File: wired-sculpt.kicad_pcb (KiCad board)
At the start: 2 copper layers, 40 x 54 mm, 39 parts, among them J1 USB Micro, J2 FFC 30pin, J3 AVR-ISP-6 - NOT FITTED, Q1 P-MOSFET, Q2 N-MOSFET, SW1 Button, SW2 JST connector, U1 ESD Protection, U2 LM2776DBVT, U3 AT90USB1286-AU, Y1 Crystal 16MHz

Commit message: Copy MPN back to Value field
This is for compatbility with the JLCPCB plugin
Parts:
- C1: value 4.7uF -> CL21A475KOFNNNE
- C10, C11, C12: value 0.1uF -> CL10B104KB8NNNC
- C2: value 0.1uF -> CL21B104KACNNNC
- C3: value 10nF -> CL21B103KBANNNC
- C4, C5, C6, C9: value 1uF -> CL10A105KA8NNNC
- C7, C8: value 16pF -> CL10C160JB8NNNC
- D1: value green led -> 150080GS75000
- J1: value USB Micro -> 10103594-0001LF
- J2: value FFC 30pin -> FFC3B07-30-T
- Q1: value P-MOSFET -> BSS84AK,215
- Q2: value N-MOSFET -> 2N7002BK
- R1, R2, R7: value 22 -> ERJ-PA3F22R0V
- R10, R6, R9: value 330 -> ERJ-3GEYJ331V
- R11, R12: value 150 -> ERJ-PA3J151V
- R3, R8: value 4.7k -> ERJ-PA3J472V
- R4: value 887k -> ERJ-3EKF8873V
- R5: value 47k -> ERJ-PA3J473V
- SW1: value Button -> FSMSM
- SW2: value JST connector -> S2B-PH-K-S(LF)(SN)
- U1: value ESD Protection -> USBLC6-2SC6
- Y1: value Crystal 16MHz -> TSX-3225 16.0000MF18X-AC0

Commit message: Change microcontroller and one FET MPN
Fixes mismatch that PCBWay flagged
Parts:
- Q2: value 2N7002BK -> 2N7002BK,215
- U3: value AT90USB1286-AU -> AT90USB1286-AUR
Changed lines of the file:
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@@
     (descr "64-Lead Plastic Thin Quad Flatpack (PF) - 14x14x1 mm Body, 2.00 mm [TQFP] (see Microchip Packaging Specification 00000049BS.pdf)")
     (tags "QFP 0.8")
-    (property "MPN" "AT90USB1286-AU")
+    (property "MPN" "AT90USB1286-AUR")
     (property "Sheetfile" "wired-sculpt.kicad_sch")
     (property "Sheetname" "")
@@
       (effects (font (size 1 1) (thickness 0.15)))
     )
-    (fp_text value "AT90USB1286-AU" (at 0 9.45) (layer "F.Fab")
+    (fp_text value "AT90USB1286-AUR" (at 0 9.45) (layer "F.Fab")
       (effects (font (size 1 1) (thickness 0.15)))
     )
@@
     (descr "SOT-23, Standard")
     (tags "SOT-23")
-    (property "MPN" "2N7002BK")
+    (property "MPN" "2N7002BK,215")
     (property "Notes" "N-MOSFET")
     (property "Sheetfile" "wired-sculpt.kicad_sch")
@@
       (effects (font (size 1 1) (thickness 0.15)))
     )
-    (fp_text value "2N7002BK" (at 0 2.5) (layer "F.Fab")
-      (effects (font (size 1 1) (thickness 0.15)))
-    )
+    (fp_text value "2N7002BK,215" (at 0 2.5) (layer "F.Fab")
+      (effects (font (size 1 1) (thickness 0.15)))
+    )

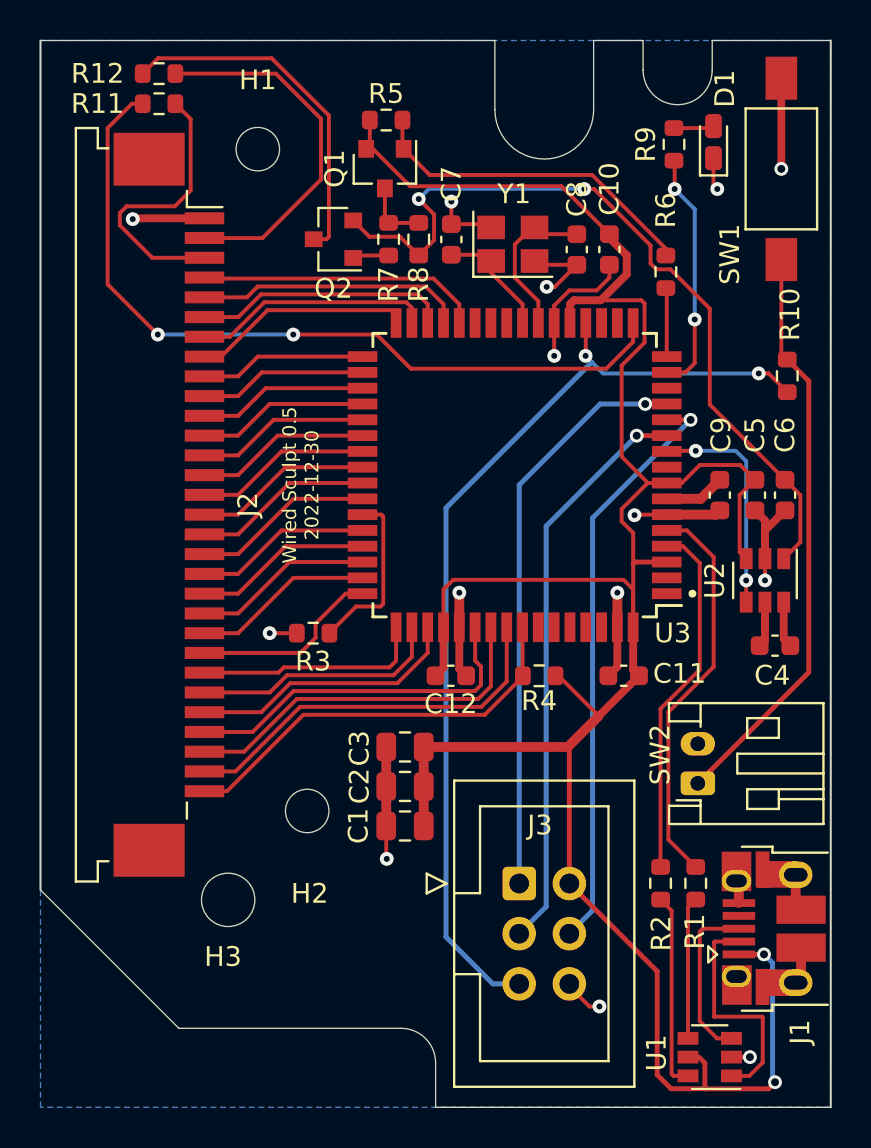
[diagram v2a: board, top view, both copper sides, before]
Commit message: Properly ground mounting pads for FFC
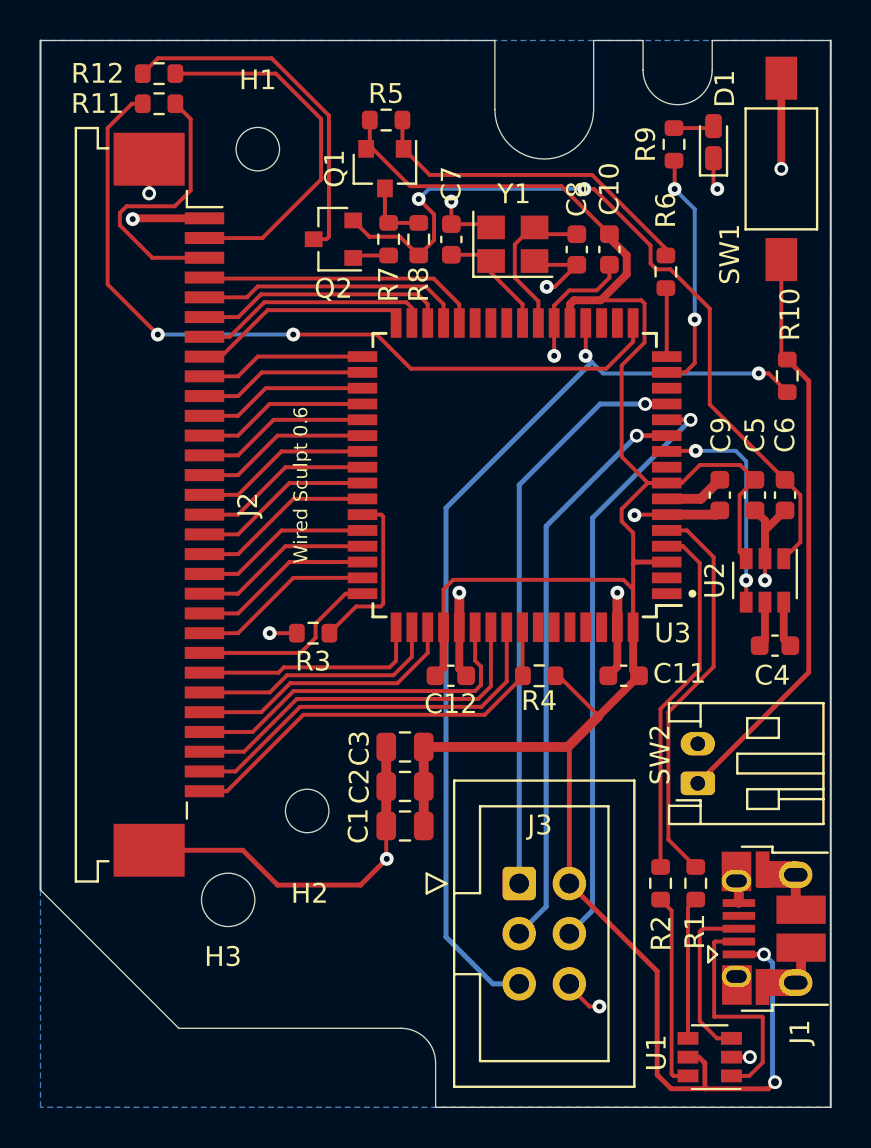
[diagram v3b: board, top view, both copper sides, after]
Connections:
- J2 pad MP: (no net) -> GND
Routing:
- net GND: track 57.1 -> 72.1 mm, vias 14 -> 15
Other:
- board text added: "Wired Sculpt 0.6"
- board text removed: "Wired Sculpt 0.5 2022-12-30"
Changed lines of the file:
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@@
     (pad "30" smd rect (at 14.5 -1.8 270) (size 0.61 2) (layers "F.Cu" "F.Paste" "F.Mask")
       (net 15 "PF4") (pinfunction "Pin_30") (pintype "passive"))
-    (pad "MP" smd rect (at -17.49 1 270) (size 2.68 3.6) (layers "F.Cu" "F.Paste" "F.Mask" "Eco2.User"))
-    (pad "MP" smd rect (at 17.49 1 270) (size 2.68 3.6) (layers "F.Cu" "F.Paste" "F.Mask"))
+    (pad "MP" smd rect (at -17.49 1 270) (size 2.68 3.6) (layers "F.Cu" "F.Paste" "F.Mask" "Eco2.User")
+      (net 1 "GND") (pinfunction "MountPin") (pintype "passive"))
+    (pad "MP" smd rect (at 17.49 1 270) (size 2.68 3.6) (layers "F.Cu" "F.Paste" "F.Mask")
+      (net 1 "GND") (pinfunction "MountPin") (pintype "passive"))
     (model "${KISYS3DMOD}/Connector_FFC-FPC.3dshapes/TE_3-84952-0_1x30-1MP_P1.0mm_Horizontal.wrl"
       (offset (xyz 0 0 0))
@@
   (gr_line (start 140 84) (end 140 81.75) (layer "Edge.Cuts") (width 0.05))
   (gr_line (start 148 30) (end 148 33.5) (layer "Edge.Cuts") (width 0.05))
-  (gr_text "Wired Sculpt 0.5\n2022-12-30" (at 133.177 52.504 90) (layer "F.SilkS")
+  (gr_text "Wired Sculpt 0.6" (at 133.177 52.504 90) (layer "F.SilkS")
     (effects (font (size 0.7 0.7) (thickness 0.1)))
   )
@@
   (segment (start 156.672 54.295) (end 156.672 56.23) (width 0.4) (layer "F.Cu") (net 1))
   (segment (start 149.2 61.701) (end 148.745 62.156) (width 0.4) (layer "F.Cu") (net 1))
+  (segment (start 136.202 72.75) (end 137.527 71.425) (width 0.25) (layer "F.Cu") (net 1))
   (segment (start 140.797 39.296) (end 142.6425 39.296) (width 0.2) (layer "F.Cu") (net 1))
   (segment (start 141.2 61.811) (end 141.545 62.156) (width 0.4) (layer "F.Cu") (net 1))
   (segment (start 149.2 59.7) (end 149.2 61.701) (width 0.4) (layer "F.Cu") (net 1))
   (segment (start 156.672 54.803) (end 156.672 56.23) (width 0.4) (layer "F.Cu") (net 1))
+  (segment (start 130.24 70.99) (end 132 72.75) (width 0.25) (layer "F.Cu") (net 1))
   (segment (start 154.975 81.46) (end 155.91 81.46) (width 0.25) (layer "F.Cu") (net 1))
   (segment (start 150.096 54) (end 150.068 54.028) (width 0.2) (layer "F.Cu") (net 1))
@@
   (segment (start 151.7 54) (end 150.096 54) (width 0.2) (layer "F.Cu") (net 1))
   (segment (start 158.23 72.23) (end 158.23 73.73) (width 0.5) (layer "F.Cu") (net 1))
+  (segment (start 125.5 36.01) (end 125.5 37.742499) (width 0.25) (layer "F.Cu") (net 1))
   (segment (start 137.5 69.76) (end 137.5 71.398) (width 0.2) (layer "F.Cu") (net 1))
   (segment (start 154.173 54) (end 151.7 54) (width 0.5) (layer "F.Cu") (net 1))
   (segment (start 141.2 59.7) (end 141.2 61.811) (width 0.4) (layer "F.Cu") (net 1))
   (segment (start 128.3 39) (end 124.71 39) (width 0.4) (layer "F.Cu") (net 1))
+  (segment (start 125.5 70.99) (end 130.24 70.99) (width 0.25) (layer "F.Cu") (net 1))
   (segment (start 146.768891 42.649989) (end 148.153791 42.649989) (width 0.2) (layer "F.Cu") (net 1))
   (segment (start 156.672 57.33) (end 156.672 56.23) (width 0.2) (layer "F.Cu") (net 1))
@@
   (segment (start 146 44.3) (end 146 43.41888) (width 0.2) (layer "F.Cu") (net 1))
   (segment (start 149.2 57.95) (end 149.2 59.7) (width 0.5) (layer "F.Cu") (net 1))
+  (segment (start 132 72.75) (end 136.202 72.75) (width 0.25) (layer "F.Cu") (net 1))
   (segment (start 154.386 53.787) (end 154.173 54) (width 0.5) (layer "F.Cu") (net 1))
   (segment (start 158.5 75.92) (end 158.5 77.42) (width 0.5) (layer "F.Cu") (net 1))
@@
   (via (at 156.672 57.33) (size 0.7) (drill 0.3) (layers "F.Cu" "B.Cu") (net 1))
   (via (at 150.068 54.028) (size 0.7) (drill 0.3) (layers "F.Cu" "B.Cu") (net 1))
+  (via (at 125.5 37.742499) (size 0.7) (drill 0.4) (layers "F.Cu" "B.Cu") (net 1))
   (via (at 137.527 71.425) (size 0.7) (drill 0.3) (layers "F.Cu" "B.Cu") (net 1))
   (via (at 141.2 57.95) (size 0.7) (drill 0.3) (layers "F.Cu" "B.Cu") (net 1))

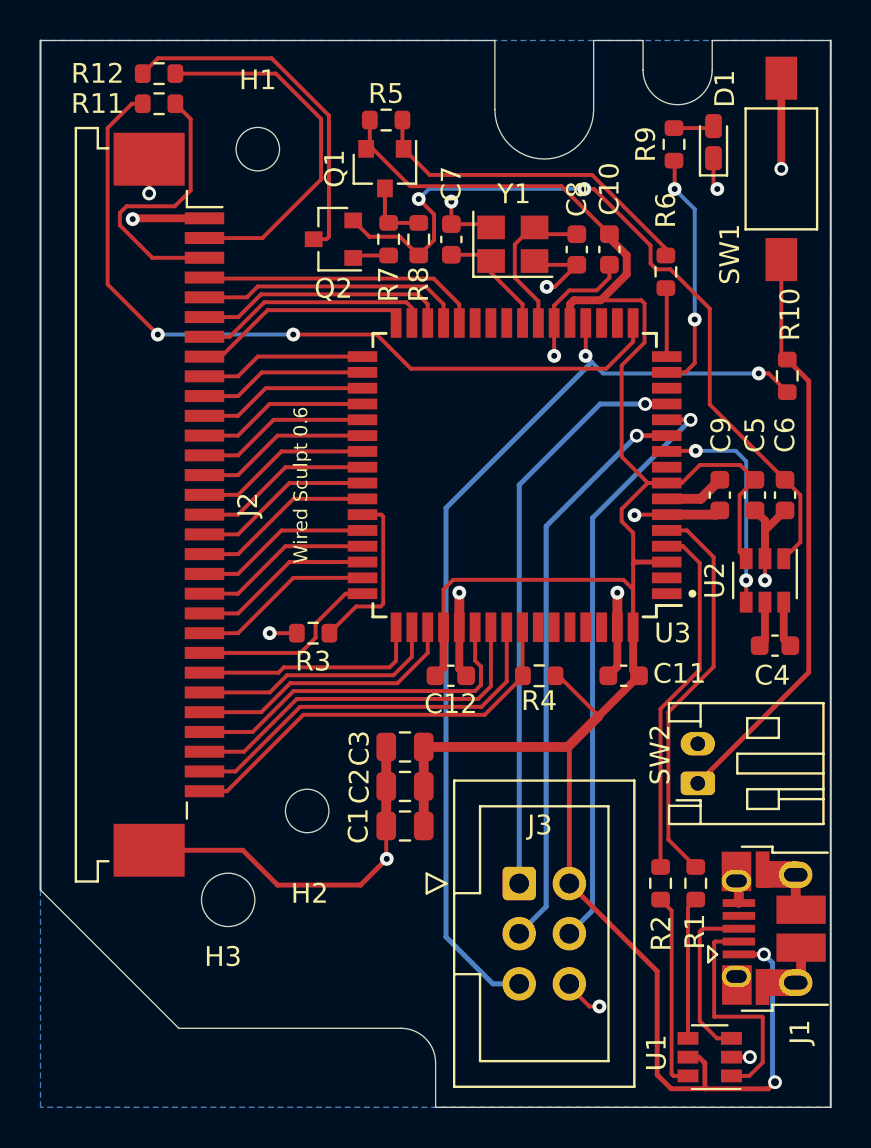
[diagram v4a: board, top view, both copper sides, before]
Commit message: Shift header down 1mm
This fits more closely to the original board
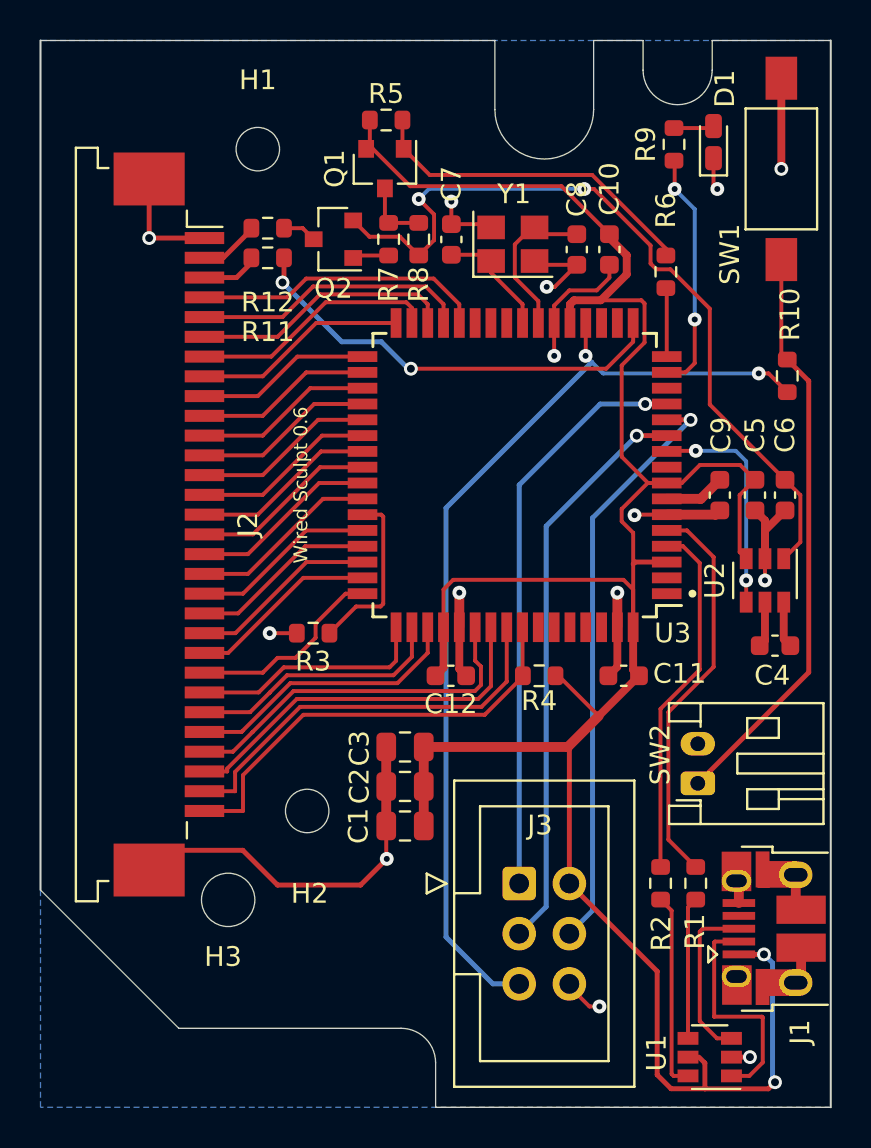
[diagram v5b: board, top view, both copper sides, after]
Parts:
- moved R12 9.56 mm to (131.5, 39.5), turned to 180 degrees
- moved R11 9.54 mm to (131.5, 41.0), turned to 180 degrees
- moved J2 1.00 mm to (126.5, 54.5)
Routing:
- net RED+: track 40.1 -> 22.4 mm
- net GREEN-: track 17.9 -> 1.73 mm
- net Net-(J2-Pad2): track 18.5 -> 3.04 mm
- net Net-(J2-Pad3): track 14.4 -> 2.69 mm
- net PF4: track 21.0 -> 22.5 mm
- net Net-(J2-Pad8): track 9.68 -> 10.8 mm
- net PF5: track 19.9 -> 20.9 mm
- net GND: track 72.1 -> 72.5 mm, vias 15 -> 14
